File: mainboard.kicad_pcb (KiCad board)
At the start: 2 copper layers, 81.3 x 72.5 mm, 57 parts, among them J1 Screw_Terminal_1x02, J2 SERVO 5V, Q1 IRLR024NPBF, U1 AT90CAN128-16MU, U2 MCP2551-I/SN, Y1 Crystal

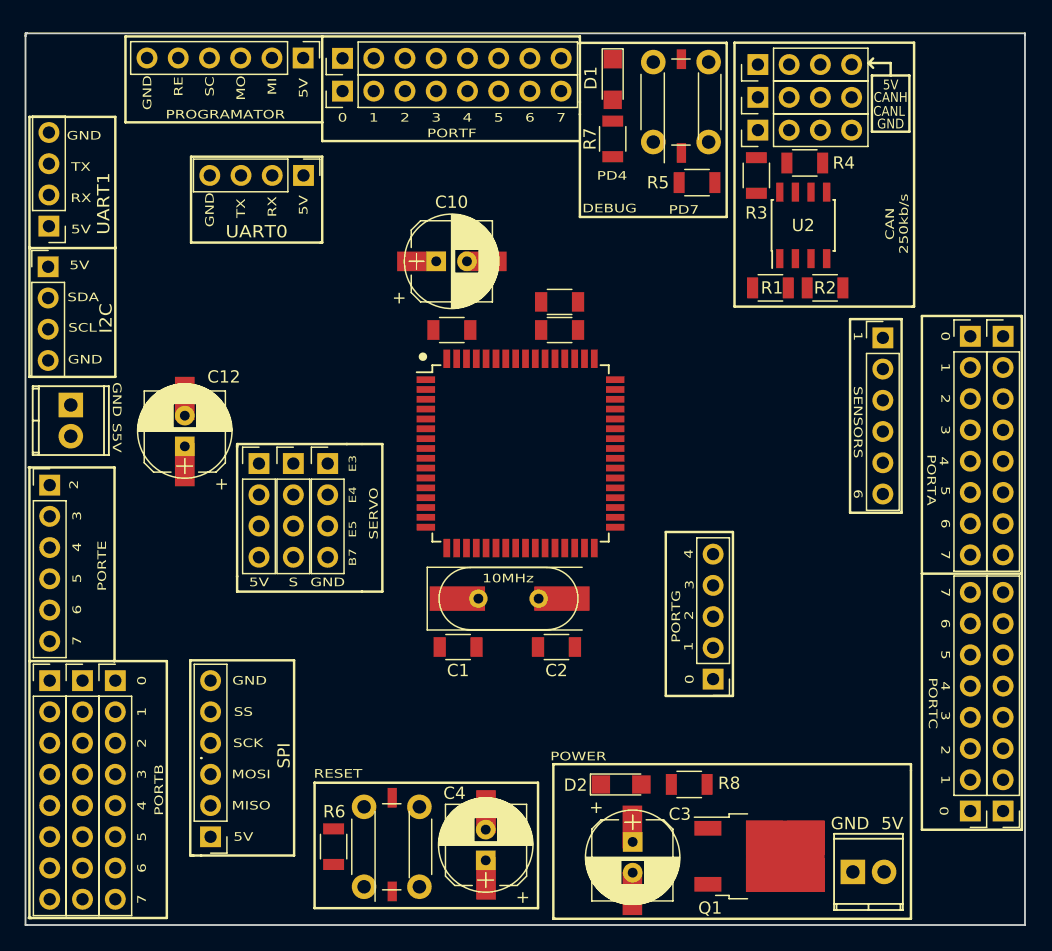
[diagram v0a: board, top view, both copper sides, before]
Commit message: Added mosfet and servo
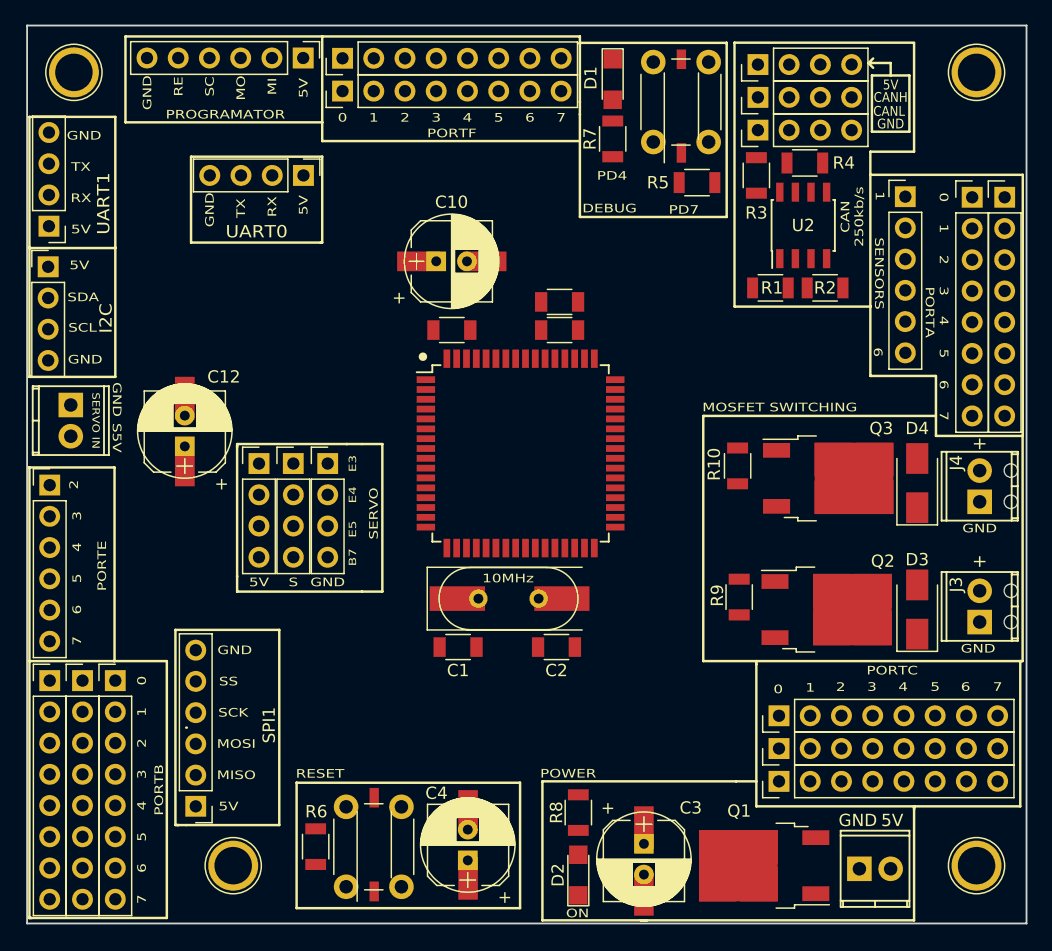
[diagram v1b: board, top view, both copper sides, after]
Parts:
- removed PG1: CONN_01X05, Pin_Headers:Pin_Header_Straight_1x05_Pitch2.54mm
- added D3: STTH2R06U, Diodes_SMD:D_SMA, F.Cu at (134.6, 83.8)
- added D4: STTH2R06U, Diodes_SMD:D_SMA, F.Cu at (134.6, 73.5)
- added J3: Screw_Terminal_1x02, Connectors_Terminal_Blocks:TerminalBlock_Pheonix_MPT-2.54mm_2pol, F.Cu at (139.7, 84.8)
- added J4: Screw_Terminal_1x02, Connectors_Terminal_Blocks:TerminalBlock_Pheonix_MPT-2.54mm_2pol, F.Cu at (139.7, 75.1)
- added PC_VCC1: CONN_01X08, Pin_Headers:Pin_Header_Straight_1x08_Pitch2.54mm, F.Cu at (123.4, 97.8)
- added Q2: IRLR024NPBF, TO_SOT_Packages_SMD:TO-252-2, F.Cu at (127.3, 83.8)
- added Q3: IRLR024NPBF, TO_SOT_Packages_SMD:TO-252-2, F.Cu at (127.4, 73.2)
- added R10: 10K, Resistors_SMD:R_1206, F.Cu at (120.0, 72.1)
- added R9: 10K, Resistors_SMD:R_1206, F.Cu at (120.1, 82.8)
- added REF**: 1pin, Connectors:1pin, F.Cu at (139.4, 104.6)
- added REF**: 1pin, Connectors:1pin, F.Cu at (139.4, 40.1)
- added REF**: 1pin, Connectors:1pin, F.Cu at (66.0, 40.1)
- added REF**: 1pin, Connectors:1pin, F.Cu at (79.0, 104.6)
- moved PC_GND1 18.9 mm to (123.4, 95.1), turned to 90 degrees
- moved PC1 17.4 mm to (123.4, 92.5), turned to 90 degrees
- moved SENSOR1 11.6 mm to (133.7, 50.2)
- moved PA1 11.3 mm to (139.1, 50.3)
- moved PA_GND1 11.3 mm to (141.7, 50.3)
- moved R8 9.30 mm to (107.1, 100.3), turned to 270 degrees
- moved D2 8.15 mm to (107.1, 105.4), turned to 90 degrees
- moved SPI1 2.75 mm to (75.9, 99.8)
- moved C11 1.46 mm to (98.1, 104.2)
- moved C4 1.46 mm to (98.1, 103.0)
- moved R6 1.46 mm to (85.7, 103.1)
- moved SW_SMD1 1.46 mm to (90.5, 102.9)
- moved SW_TH1 1.46 mm to (88.2, 106.4)
- moved C3 0.94 mm to (112.4, 104.3)
- moved C9 0.93 mm to (112.4, 102.9)
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- renumbered SPI to SPI1
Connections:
- Q1 pad 2: Net-(J1-Pad1) -> GND
- Q1 pad 3: GND -> Net-(J1-Pad1)
- U1 pad 18: PG3 -> (no net)
- U1 pad 19: PG4 -> (no net)
- U1 pad 43: PG2 -> (no net)
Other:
- board size 81.3 x 72.5 mm -> 81.3 x 73 mm
- board text added: "+"
- board text added: "MOSFET SWITCHING"
- board text added: "ON"
- board text added: "SERVO IN"
- board text removed: "PORTG"

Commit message: Added some bottom paste
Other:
- board text added: "PC"
- board text added: "PF"
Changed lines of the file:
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@@
     (area 62.154999 36.246999 143.585001 109.422001)
     (thickness 1.6)
-    (drawings 206)
+    (drawings 231)
     (tracks 0)
     (zones 0)
@@
     (pad 1 thru_hole circle (at 0 0) (size 4.064 4.064) (drill 3.048) (layers *.Cu *.Mask))
   )
+  (gr_text 5V (at 66.294 85.6615) (layer B.Paste)
+    (effects (font (size 0.7 0.8) (thickness 0.175)) (justify mirror))
+  )
+  (gr_text GND (at 68.7705 85.6615) (layer B.Paste)
+    (effects (font (size 0.7 0.8) (thickness 0.175)) (justify mirror))
+  )
+  (gr_text PC (at 71.501 85.6615) (layer B.Paste)
+    (effects (font (size 0.7 0.8) (thickness 0.175)) (justify mirror))
+  )
+  (gr_line (start 69.4055 88.265) (end 71.3105 86.36) (angle 90) (layer B.Paste) (width 0.2))
+  (gr_line (start 66.675 88.265) (end 68.6435 86.2965) (angle 90) (layer B.Paste) (width 0.2))
+  (gr_line (start 64.135 88.265) (end 66.1035 86.2965) (angle 90) (layer B.Paste) (width 0.2))
+  (gr_line (start 62.738 108.712) (end 62.738 88.265) (angle 90) (layer B.Paste) (width 0.2))
+  (gr_line (start 70.8025 108.712) (end 62.738 108.712) (angle 90) (layer B.Paste) (width 0.2))
+  (gr_line (start 70.8025 88.265) (end 70.8025 108.712) (angle 90) (layer B.Paste) (width 0.2))
+  (gr_line (start 62.738 88.265) (end 70.8025 88.265) (angle 90) (layer B.Paste) (width 0.2))
+  (gr_text 5V (at 120.396 97.79) (layer B.Paste)
+    (effects (font (size 1.5 1.5) (thickness 0.3)) (justify mirror))
+  )
+  (gr_text PC (at 120.396 92.456) (layer B.Paste)
+    (effects (font (size 1.5 1.5) (thickness 0.3)) (justify mirror))
+  )
+  (gr_text GND (at 119.634 94.996) (layer B.Paste)
+    (effects (font (size 1.5 1.5) (thickness 0.3)) (justify mirror))
+  )
+  (gr_text PF (at 108.966 41.402) (layer B.Paste)
+    (effects (font (size 1.5 1.5) (thickness 0.3)) (justify mirror))
+  )
+  (gr_text GND (at 109.728 38.608) (layer B.Paste)
+    (effects (font (size 1.5 1.5) (thickness 0.3)) (justify mirror))
+  )
+  (gr_line (start 86.614 37.592) (end 86.614 37.719) (angle 90) (layer B.Paste) (width 0.2))
+  (gr_line (start 107.061 37.592) (end 86.614 37.592) (angle 90) (layer B.Paste) (width 0.2))
+  (gr_line (start 107.061 42.926) (end 107.061 37.592) (angle 90) (layer B.Paste) (width 0.2))
+  (gr_line (start 86.614 42.926) (end 107.061 42.926) (angle 90) (layer B.Paste) (width 0.2))
+  (gr_line (start 86.614 37.592) (end 86.614 42.926) (angle 90) (layer B.Paste) (width 0.2))
+  (gr_line (start 122.047 91.059) (end 122.174 91.059) (angle 90) (layer B.Paste) (width 0.2))
+  (gr_line (start 122.047 99.187) (end 122.047 91.059) (angle 90) (layer B.Paste) (width 0.2))
+  (gr_line (start 142.494 99.187) (end 122.047 99.187) (angle 90) (layer B.Paste) (width 0.2))
+  (gr_line (start 142.494 91.059) (end 142.494 99.187) (angle 90) (layer B.Paste) (width 0.2))
+  (gr_line (start 122.047 91.059) (end 142.494 91.059) (angle 90) (layer B.Paste) (width 0.2))
   (gr_text "MOSFET SWITCHING" (at 123.444 67.3735) (layer F.SilkS)
     (effects (font (size 0.7 0.9) (thickness 0.125)))

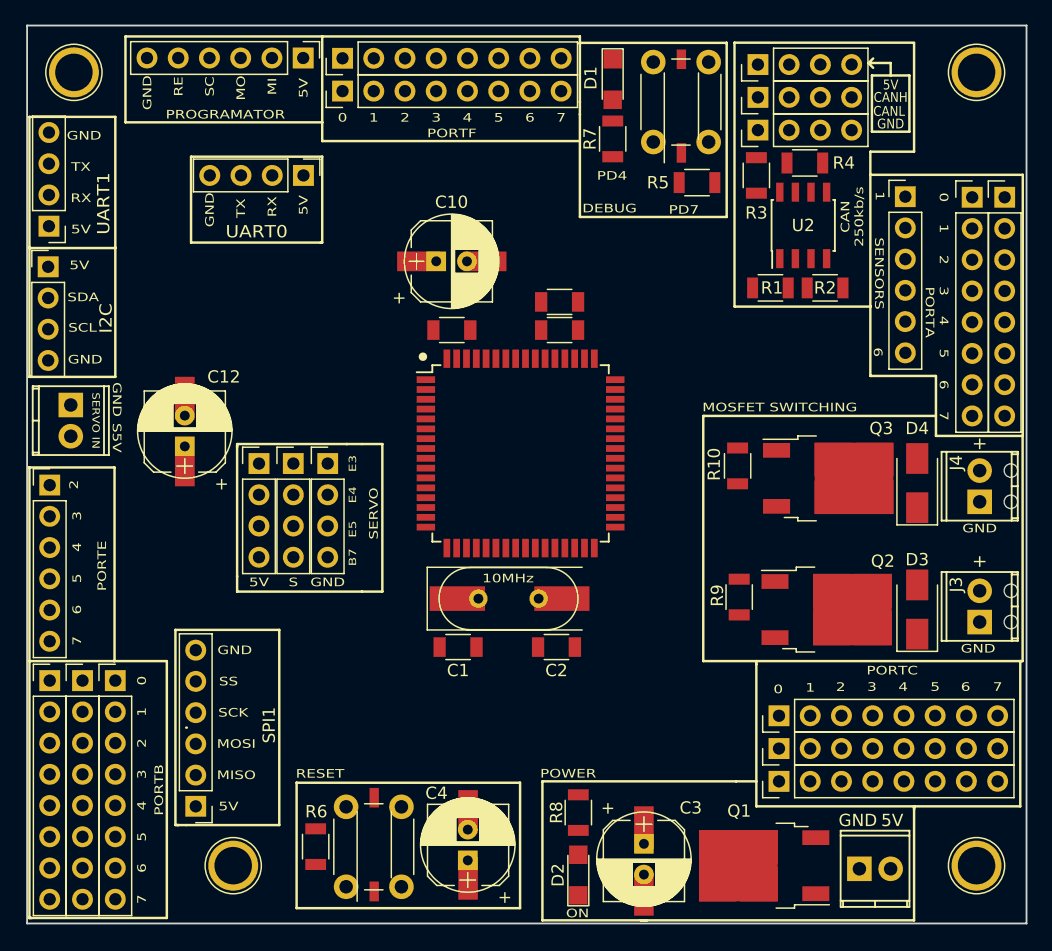
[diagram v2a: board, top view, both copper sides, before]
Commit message: Modified alot of stuff, added module and power for servo
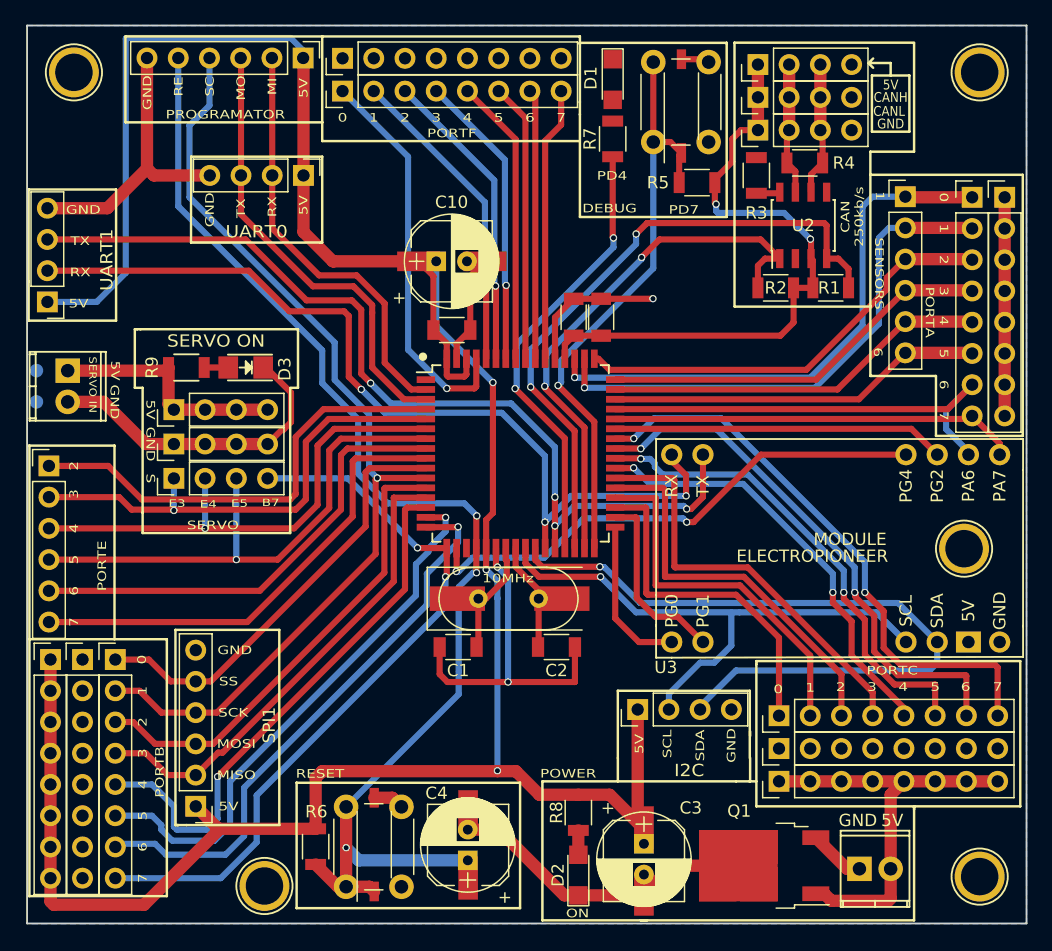
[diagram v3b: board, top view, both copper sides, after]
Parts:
- removed C12: 100u, Capacitors_THT:CP_Radial_D7.5mm_P2.50mm
- removed C13: 100u, Capacitors_SMD:CP_Elec_6.3x4.5
- removed D4: STTH2R06U, Diodes_SMD:D_SMA
- removed J3, J4: Screw_Terminal_1x02, Connectors_Terminal_Blocks:TerminalBlock_Pheonix_MPT-2.54mm_2pol
- removed Q2, Q3: IRLR024NPBF, TO_SOT_Packages_SMD:TO-252-2
- removed R10: 10K, Resistors_SMD:R_1206
- removed the REF** at (139.4, 104.6)
- removed the REF** at (139.4, 40.1)
- removed the REF** at (66.0, 40.1)
- removed the REF** at (79.0, 104.6)
- added REF**: 1pin, Connect:1pin, F.Cu at (139.7, 40.1)
- added REF**: 1pin, Connect:1pin, F.Cu at (138.4, 78.9)
- added REF**: 1pin, Connect:1pin, F.Cu at (139.7, 105.5)
- added REF**: 1pin, Connect:1pin, F.Cu at (81.5, 106.3)
- added U3: EP_MODULE, EP_Module:EP_Module, F.Cu at (114.7, 83.9)
- added eREF**: 1pin, Connect:1pin, F.Cu at (66.0, 40.1)
- D3: value STTH2R06U -> LED; footprint Diodes_SMD:D_SMA -> LEDs:LED_1206
- R9: value 10K -> 1K
- moved I2C1 60.0 mm to (111.9, 91.9), turned to 90 degrees
- moved D3 58.0 mm to (80.0, 64.1), turned to 180 degrees
- moved R9 48.7 mm to (75.2, 64.1), turned to 0 degrees
- moved SERVO_GND1 12.6 mm to (74.2, 70.4), turned to 90 degrees
- moved SERVO1 9.79 mm to (74.2, 73.2), turned to 90 degrees
- moved SERO_5V1 8.19 mm to (74.2, 67.6), turned to 90 degrees
- moved UART1 6.16 mm to (63.9, 58.8)
- moved R1 4.90 mm to (127.6, 57.7), turned to 0 degrees
- moved R2 4.01 mm to (123.1, 57.7), turned to 180 degrees
- moved C8 3.60 mm to (108.9, 60.0), turned to 90 degrees
- moved J2 2.81 mm to (65.5, 64.4)
- moved PB_VCC1 1.72 mm to (64.1, 87.9)
- moved PB1 1.71 mm to (69.4, 87.9)
- moved PB_GND1 1.71 mm to (66.7, 87.9)
- moved PE1 1.56 mm to (64.0, 72.1)
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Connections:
- D1 pad 1: GND -> (no net)
- D1 pad 2: Net-(D1-Pad2) -> (no net)
- D3 pad 1: Net-(D3-Pad1) -> GND
- I2C1 pad 2: SDA -> SCL
- I2C1 pad 3: SCL -> SDA
- J2 pad 1: GND -> +5C
- J2 pad 2: +5C -> GND
- R7 pad 2: Net-(D1-Pad2) -> (no net)
- R9 pad 1: PG0 -> +5C
- R9 pad 2: GND -> Net-(D3-Pad2)
- U1 pad 18: (no net) -> PG3
- U1 pad 43: (no net) -> PG2
- U2 pad 1: TXCAN -> RXCAN
- U2 pad 4: RXCAN -> TXCAN
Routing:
- net +5V: track 0.00 -> 307.0 mm, vias 0 -> 5
- net GND: track 0.00 -> 149.8 mm, vias 0 -> 3
- net RESET: track 0.00 -> 101.7 mm, vias 0 -> 4
- net PB1: track 0.00 -> 78.6 mm, vias 0 -> 1
- net TXD1: track 0.00 -> 76.2 mm, vias 0 -> 4
- net RXD1: track 0.00 -> 73.3 mm, vias 0 -> 3
- net PB7: track 0.00 -> 60.0 mm, vias 0 -> 3
- net SDA: track 0.00 -> 59.1 mm, vias 0 -> 1
- net TXCAN: track 0.00 -> 52.9 mm, vias 0 -> 2
- net PD7: track 0.00 -> 49.1 mm, vias 0 -> 1
- net PC7: track 0.00 -> 47.3 mm, vias 0 -> 2
- net PB6: track 0.00 -> 47.0 mm, vias 0 -> 1
- net PA0: track 0.00 -> 45.7 mm, vias 0 -> 1
- net SCL: track 0.00 -> 45.5 mm, vias 0 -> 1
- net PB5: track 0.00 -> 44.8 mm, vias 0 -> 1
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- added copper zone on B.Cu, net GND
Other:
- net class Default2 added: clearance 0.2, trace_width 1, via_dia 0.6, via_drill 0.4
- board text added: "Main Board V1"
- board text added: "PB"
- board text added: "SERVO ON"
- board text added: "http://elektropioneer.co.rs/ https://github.com/Elektropioneer"
- board text removed: "+"
- board text removed: "MOSFET SWITCHING"
- board text removed: "S5V"

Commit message: Modifyed positions around U3
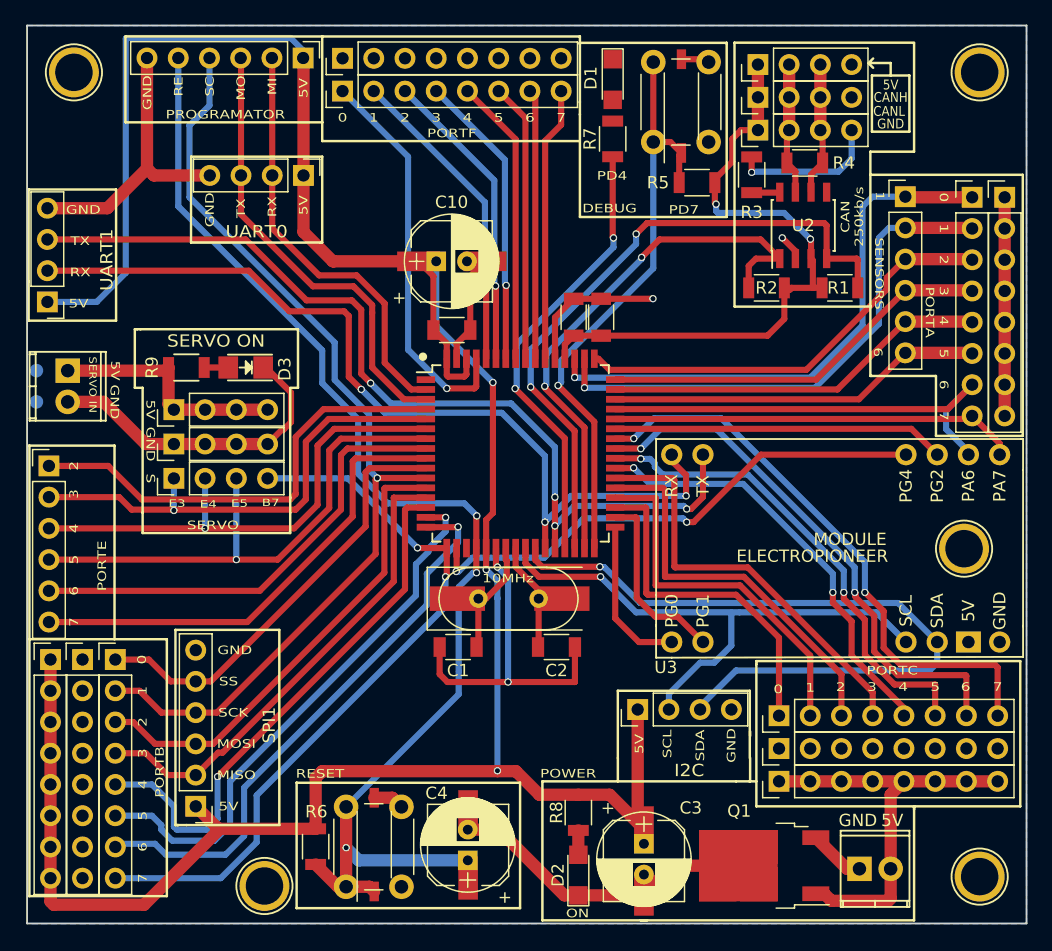
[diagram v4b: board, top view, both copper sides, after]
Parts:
- moved R1 0.75 mm to (128.3, 57.7)
- moved R2 0.75 mm to (122.4, 57.7)
- moved R3 0.38 mm to (121.2, 48.5)
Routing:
- net GND: track 149.8 -> 164.1 mm, vias 3 -> 5
- net +5V: track 307.0 -> 308.3 mm
- net TXCAN: track 52.9 -> 54.1 mm
- net RXCAN: track 44.5 -> 45.3 mm
